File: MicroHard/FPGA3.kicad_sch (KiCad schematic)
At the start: 19 parts, among them J4 FPGA_DEBUG, U5 XC7A100T-FTG256

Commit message: feat: completed schematic draft
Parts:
- J4: footprint (none) -> MicroHard:MOLEX_87832-1420
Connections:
- net DONE renamed FPGA_DONE
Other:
- note removed: "Are these pull ups neccessary"
- note removed: "Very unsure here"
- moved on the sheet: D2, R22, TP2
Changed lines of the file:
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@@
 	)
 	(junction
-		(at 160.02 69.85)
+		(at 156.21 69.85)
 		(diameter 0)
 		(color 0 0 0 0)
@@
 	(wire
 		(pts
-			(xy 175.26 53.34) (xy 175.26 24.13)
+			(xy 151.13 69.85) (xy 156.21 69.85)
 		)
 		(stroke
@@
 	(wire
 		(pts
-			(xy 69.85 147.32) (xy 76.2 147.32)
+			(xy 175.26 53.34) (xy 175.26 24.13)
 		)
 		(stroke
@@
 	(wire
 		(pts
-			(xy 160.02 66.04) (xy 160.02 69.85)
+			(xy 69.85 147.32) (xy 76.2 147.32)
 		)
 		(stroke
@@
 	(wire
 		(pts
-			(xy 38.1 154.94) (xy 48.26 154.94)
+			(xy 156.21 66.04) (xy 156.21 69.85)
 		)
 		(stroke
@@
 	(wire
 		(pts
-			(xy 148.59 74.93) (xy 153.67 74.93)
+			(xy 38.1 154.94) (xy 48.26 154.94)
 		)
 		(stroke
@@
 	(wire
 		(pts
-			(xy 151.13 69.85) (xy 160.02 69.85)
+			(xy 148.59 74.93) (xy 153.67 74.93)
 		)
 		(stroke
@@
 	(wire
 		(pts
-			(xy 160.02 69.85) (xy 167.64 69.85)
+			(xy 156.21 69.85) (xy 158.75 69.85)
 		)
 		(stroke
@@
 	(wire
 		(pts
-			(xy 59.69 125.73) (xy 66.04 125.73)
+			(xy 66.04 129.54) (xy 72.39 129.54)
 		)
 		(stroke
@@
 	(wire
 		(pts
-			(xy 29.21 125.73) (xy 39.37 125.73)
+			(xy 38.1 129.54) (xy 45.72 129.54)
 		)
 		(stroke
@@
 	(wire
 		(pts
-			(xy 52.07 125.73) (xy 46.99 125.73)
+			(xy 58.42 129.54) (xy 53.34 129.54)
 		)
 		(stroke
@@
 	(wire
 		(pts
-			(xy 107.95 57.15) (xy 118.11 57.15)
+			(xy 107.95 57.15) (xy 116.84 57.15)
 		)
 		(stroke
@@
 		)
 	)
-	(text "Very unsure here\n"
-		(exclude_from_sim no)
-		(at 157.226 99.314 0)
-		(effects
-			(font
-				(size 1.27 1.27)
-			)
-		)
-	)
-	(text "Are these pull ups neccessary"
-		(exclude_from_sim no)
-		(at 235.712 49.276 0)
-		(effects
-			(font
-				(size 1.27 1.27)
-			)
-		)
-	)
 	(label "JTAG_TDI"
 		(at 115.57 44.45 0)
@@
 		)
 	)
+	(label "VCC0_0"
+		(at 252.73 49.53 90)
+		(fields_autoplaced yes)
+		(effects
+			(font
+				(size 1.27 1.27)
+			)
+			(justify left bottom)
+		)
+	)
 	(label "JTAG_TDI"
 		(at 227.33 73.66 180)
@@
 		)
 	)
-	(label "DONE"
-		(at 29.21 125.73 180)
+	(label "VCC0_0"
+		(at 118.11 80.01 0)
 		(fields_autoplaced yes)
 		(effects
@@
 				(size 1.27 1.27)
 			)
-			(justify right bottom)
+			(justify left bottom)
 		)
 	)
-	(label "DONE"
-		(at 167.64 69.85 0)
+	(label "VCC0_0"
+		(at 167.64 92.71 0)
 		(fields_autoplaced yes)
 		(effects
@@
 		)
 	)
-	(label "VCC0_0"
-		(at 167.64 92.71 0)
+	(global_label "FPGA_DONE"
+		(shape output)
+		(at 158.75 69.85 0)
 		(fields_autoplaced yes)
 		(effects
@@
 				(size 1.27 1.27)
 			)
-			(justify left bottom)
+			(justify left)
+		)
+		(property "Intersheetrefs" "${INTERSHEET_REFS}"
+			(at 172.5 69.85 0)
+			(effects
+				(font
+					(size 1.27 1.27)
+				)
+				(justify left)
+				(hide yes)
+			)
 		)
 	)
@@
 		)
 	)
-	(global_label "+3.3V"
+	(global_label "FPGA_LED2"
 		(shape input)
-		(at 118.11 80.01 0)
+		(at 38.1 154.94 180)
 		(fields_autoplaced yes)
 		(effects
@@
 				(size 1.27 1.27)
 			)
-			(justify left)
+			(justify right)
 		)
 		(property "Intersheetrefs" "${INTERSHEET_REFS}"
-			(at 126.78 80.01 0)
+			(at 24.7734 154.94 0)
 			(effects
 				(font
 					(size 1.27 1.27)
 				)
-				(justify left)
+				(justify right)
 				(hide yes)
 			)
 		)
 	)
-	(global_label "FPGA_LED2"
+	(global_label "FPGA_DONE"
 		(shape input)
-		(at 38.1 154.94 180)
+		(at 38.1 129.54 180)
 		(fields_autoplaced yes)
 		(effects
@@
 		)
 		(property "Intersheetrefs" "${INTERSHEET_REFS}"
-			(at 24.7734 154.94 0)
+			(at 24.35 129.54 0)
 			(effects
 				(font
@@
 		)
 	)
-	(global_label "+3.3V"
+	(global_label "FPGA_LED1"
 		(shape input)
-		(at 252.73 49.53 90)
+		(at 38.1 147.32 180)
 		(fields_autoplaced yes)
 		(effects
@@
 				(size 1.27 1.27)
 			)
-			(justify left)
+			(justify right)
 		)
 		(property "Intersheetrefs" "${INTERSHEET_REFS}"
-			(at 252.73 40.86 90)
+			(at 24.7734 147.32 0)
 			(effects
 				(font
 					(size 1.27 1.27)
 				)
-				(justify left)
+				(justify right)
 				(hide yes)
 			)
 		)
 	)
-	(global_label "FPGA_LED1"
-		(shape input)
-		(at 38.1 147.32 180)
+	(global_label "FPGA_CONFIG_CLOCK"
+		(shape output)
+		(at 116.84 57.15 0)
 		(fields_autoplaced yes)
 		(effects
@@
 				(size 1.27 1.27)
 			)
-			(justify right)
+			(justify left)
 		)
 		(property "Intersheetrefs" "${INTERSHEET_REFS}"
-			(at 24.7734 147.32 0)
+			(at 139.5406 57.15 0)
 			(effects
 				(font
 					(size 1.27 1.27)
 				)
-				(justify right)
+				(justify left)
 				(hide yes)
 			)
 		)
 	)
-	(hierarchical_label "FPGA_CONFIG_CLOCK"
-		(shape input)
-		(at 118.11 57.15 0)
-		(fields_autoplaced yes)
-		(effects
-			(font
-				(size 1.27 1.27)
-			)
-			(justify left)
-		)
-	)
 	(hierarchical_label "FPGA_RESET"
 		(shape input)
@@
 	(symbol
 		(lib_id "Device:R")
-		(at 43.18 125.73 90)
+		(at 49.53 129.54 90)
 		(unit 1)
 		(exclude_from_sim no)
@@
 		(fields_autoplaced yes)
 		(property "Reference" "R22"
-			(at 43.18 119.38 90)
+			(at 49.53 123.19 90)
 			(effects
 				(font
@@
 		)
 		(property "Value" "100"
-			(at 43.18 121.92 90)
+			(at 49.53 125.73 90)
 			(effects
 				(font
@@
 		)
 		(property "Footprint" ""
-			(at 43.18 127.508 90)
+			(at 49.53 131.318 90)
 			(effects
 				(font
@@
 		)
 		(property "Datasheet" "~"
-			(at 43.18 125.73 0)
+			(at 49.53 129.54 0)
 			(effects
 				(font
@@
 		)
 		(property "Description" "Resistor"
-			(at 43.18 125.73 0)
+			(at 49.53 129.54 0)
 			(effects
 				(font
@@
 	(symbol
 		(lib_id "Device:LED")
-		(at 55.88 125.73 180)
+		(at 62.23 129.54 180)
 		(unit 1)
 		(exclude_from_sim no)
@@
 		(fields_autoplaced yes)
 		(property "Reference" "D2"
-			(at 57.4675 118.11 0)
+			(at 63.8175 121.92 0)
 			(effects
 				(font
@@
 		)
 		(property "Value" "LED"
-			(at 57.4675 120.65 0)
+			(at 63.8175 124.46 0)
 			(effects
 				(font
@@
 		)
 		(property "Footprint" ""
-			(at 55.88 125.73 0)
+			(at 62.23 129.54 0)
 			(effects
 				(font
@@
 		)
 		(property "Datasheet" "~"
-			(at 55.88 125.73 0)
+			(at 62.23 129.54 0)
 			(effects
 				(font
@@
 		)
 		(property "Description" "Light emitting diode"
-			(at 55.88 125.73 0)
+			(at 62.23 129.54 0)
 			(effects
 				(font
@@
 	(symbol
 		(lib_id "power:GND")
-		(at 66.04 125.73 90)
+		(at 72.39 129.54 90)
 		(unit 1)
 		(exclude_from_sim no)
@@
 		(fields_autoplaced yes)
 		(property "Reference" "#PWR031"
-			(at 72.39 125.73 0)
+			(at 78.74 129.54 0)
 			(effects
 				(font
@@
 		)
 		(property "Value" "GND"
-			(at 69.85 125.7299 90)
+			(at 76.2 129.5399 90)
 			(effects
 				(font
@@
 		)
 		(property "Footprint" ""
-			(at 66.04 125.73 0)
+			(at 72.39 129.54 0)
 			(effects
 				(font
@@
 		)
 		(property "Datasheet" ""
-			(at 66.04 125.73 0)
+			(at 72.39 129.54 0)
 			(effects
 				(font
@@
 		)
 		(property "Description" "Power symbol creates a global label with name \"GND\" , ground"
-			(at 66.04 125.73 0)
+			(at 72.39 129.54 0)
 			(effects
 				(font
@@
 			)
 		)
-		(property "Footprint" ""
+		(property "Footprint" "MicroHard:MOLEX_87832-1420"
 			(at 270.51 71.12 0)
 			(effects
@@
 	(symbol
 		(lib_id "Connector:TestPoint")
-		(at 160.02 66.04 0)
+		(at 156.21 66.04 0)
 		(unit 1)
 		(exclude_from_sim no)
@@
 		(fields_autoplaced yes)
 		(property "Reference" "TP2"
-			(at 162.56 61.4679 0)
+			(at 158.75 61.4679 0)
 			(effects
 				(font
@@
 		)
 		(property "Value" "TestPoint"
-			(at 162.56 64.0079 0)
+			(at 158.75 64.0079 0)
 			(effects
 				(font
@@
 		)
 		(property "Footprint" ""
-			(at 165.1 66.04 0)
+			(at 161.29 66.04 0)
 			(effects
 				(font
@@
 		)
 		(property "Datasheet" "~"
-			(at 165.1 66.04 0)
+			(at 161.29 66.04 0)
 			(effects
 				(font
@@
 		)
 		(property "Description" "test point"
-			(at 160.02 66.04 0)
+			(at 156.21 66.04 0)
 			(effects
 				(font

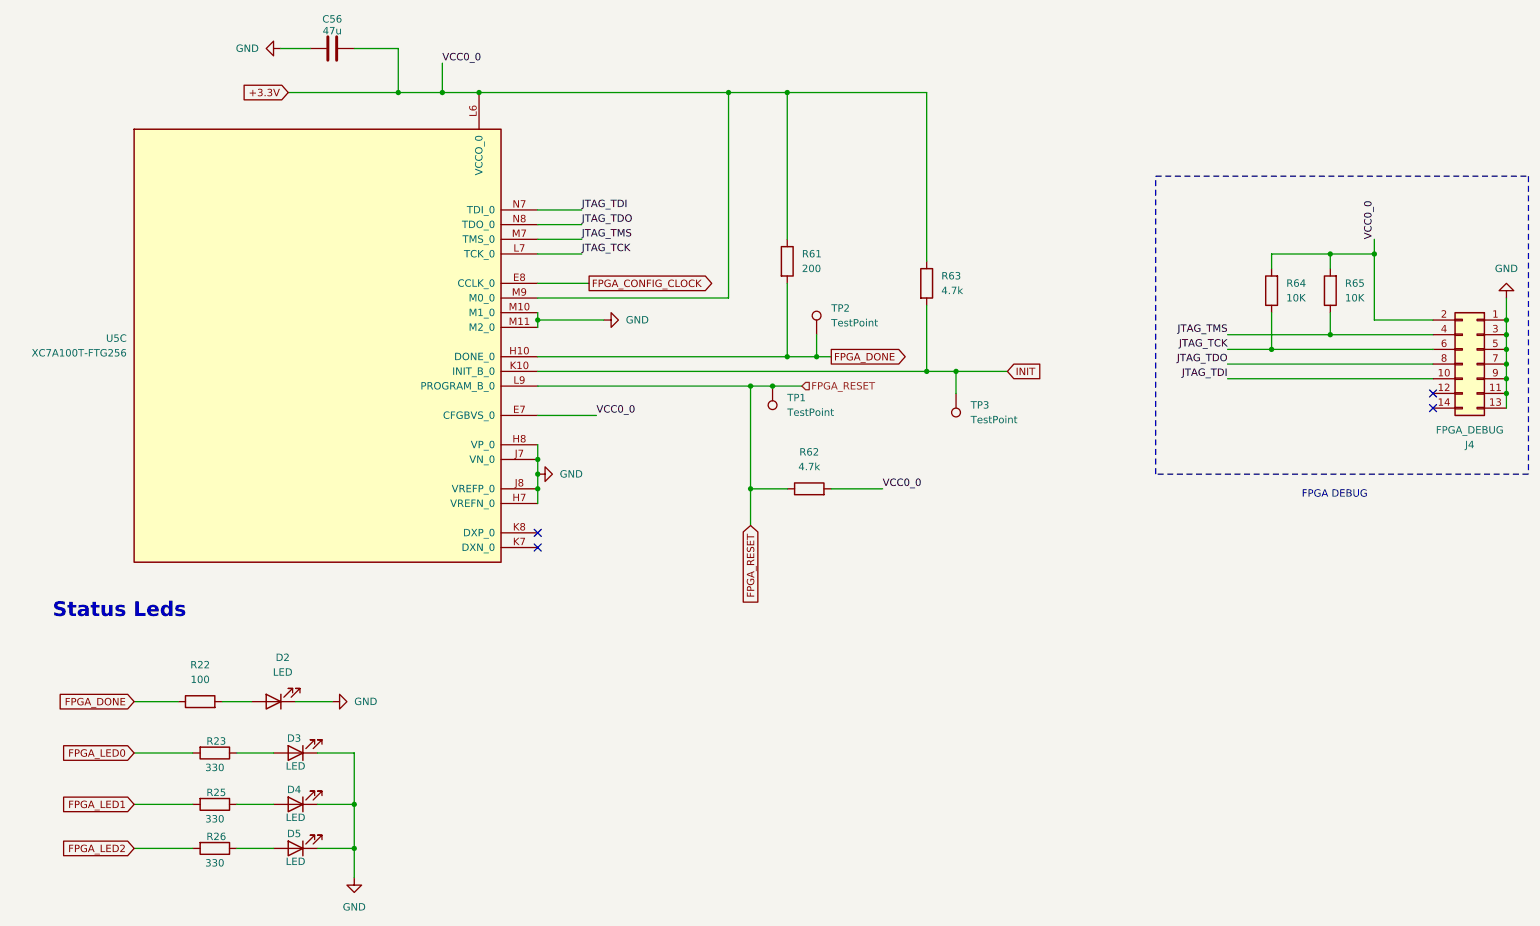
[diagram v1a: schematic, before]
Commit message: Renumber parts
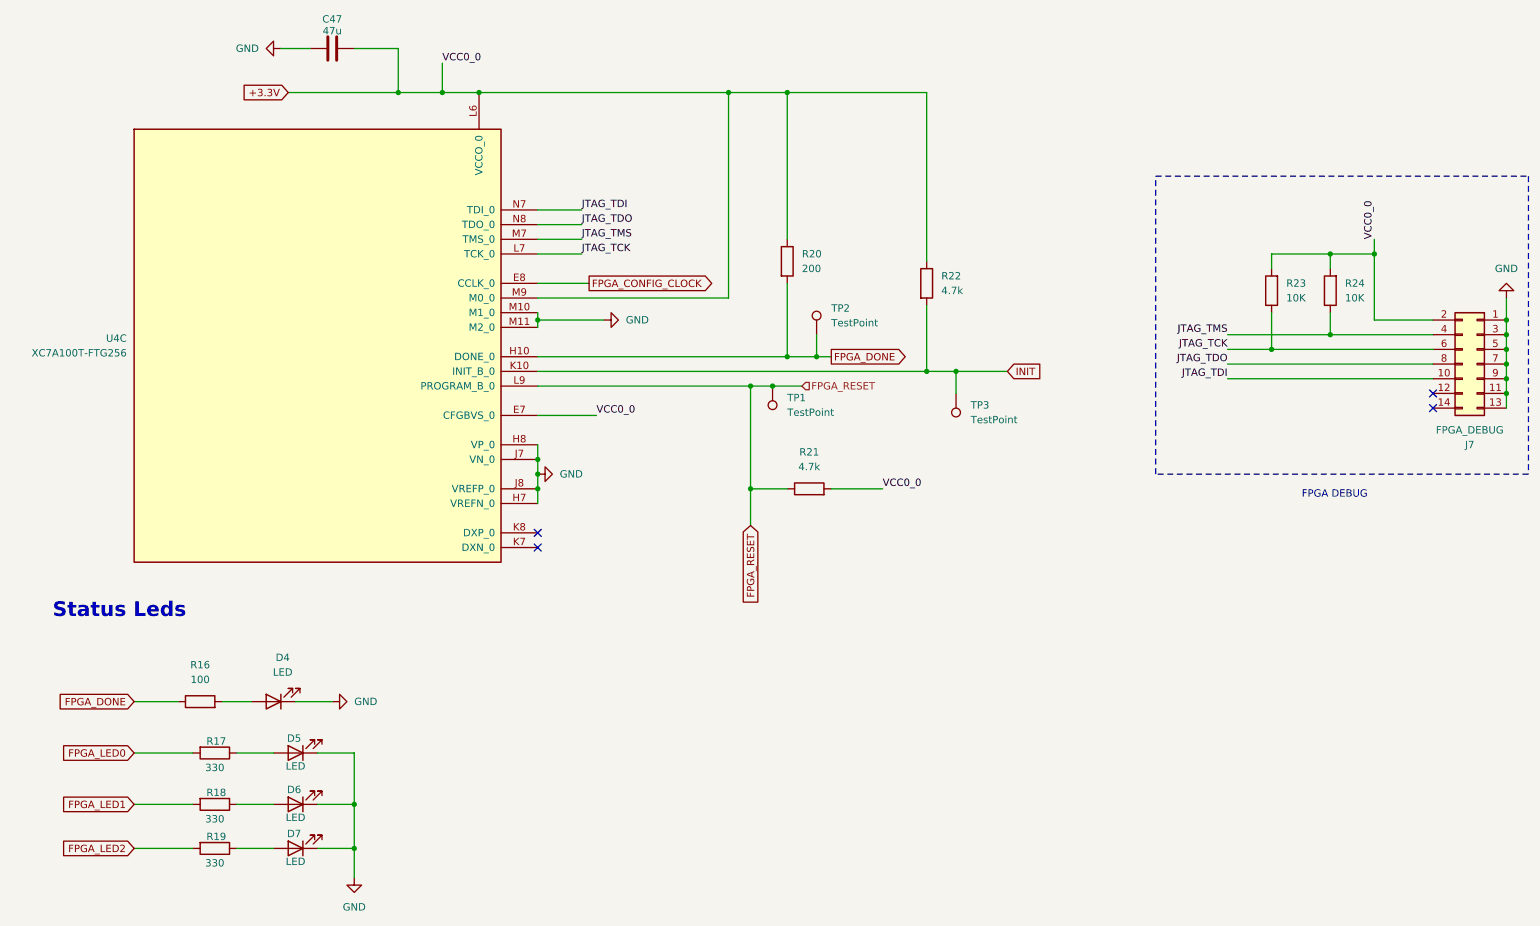
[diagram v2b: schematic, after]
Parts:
- renumbered C56 to C47, D2 to D4, D3 to D5, D4 to D6, D5 to D7, J4 to J7, R22 to R16, R23 to R17, R25 to R18, R26 to R19, R61 to R20, R62 to R21, R63 to R22, R64 to R23, R65 to R24, U5 to U4
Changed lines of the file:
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@@
 		(dnp no)
 		(fields_autoplaced yes)
-		(property "Reference" "R63"
+		(property "Reference" "R22"
 			(at 177.8 55.8799 0)
 			(effects
@@
 			(project ""
 				(path "/578bd531-a491-4b15-a479-460d159ffc14/e381883e-e672-4900-88a5-08b94f970a88/5897012d-c01f-459a-b65a-eba111a7dafb"
-					(reference "R63")
+					(reference "R22")
 					(unit 1)
 				)
@@
 		(dnp no)
 		(fields_autoplaced yes)
-		(property "Reference" "R61"
+		(property "Reference" "R20"
 			(at 153.67 52.0699 0)
 			(effects
@@
 			(project ""
 				(path "/578bd531-a491-4b15-a479-460d159ffc14/e381883e-e672-4900-88a5-08b94f970a88/5897012d-c01f-459a-b65a-eba111a7dafb"
-					(reference "R61")
+					(reference "R20")
 					(unit 1)
 				)
@@
 		(dnp no)
 		(fields_autoplaced yes)
-		(property "Reference" "R64"
+		(property "Reference" "R23"
 			(at 237.49 57.1499 0)
 			(effects
@@
 			(project ""
 				(path "/578bd531-a491-4b15-a479-460d159ffc14/e381883e-e672-4900-88a5-08b94f970a88/5897012d-c01f-459a-b65a-eba111a7dafb"
-					(reference "R64")
+					(reference "R23")
 					(unit 1)
 				)
@@
 		(dnp no)
 		(fields_autoplaced yes)
-		(property "Reference" "R22"
+		(property "Reference" "R16"
 			(at 49.53 123.19 90)
 			(effects
@@
 			(project ""
 				(path "/578bd531-a491-4b15-a479-460d159ffc14/e381883e-e672-4900-88a5-08b94f970a88/5897012d-c01f-459a-b65a-eba111a7dafb"
-					(reference "R22")
+					(reference "R16")
 					(unit 1)
 				)
@@
 		(on_board yes)
 		(dnp no)
-		(property "Reference" "R26"
+		(property "Reference" "R19"
 			(at 52.324 152.908 90)
 			(effects
@@
 			(project "MicroHard"
 				(path "/578bd531-a491-4b15-a479-460d159ffc14/e381883e-e672-4900-88a5-08b94f970a88/5897012d-c01f-459a-b65a-eba111a7dafb"
-					(reference "R26")
+					(reference "R19")
 					(unit 1)
 				)
@@
 		(dnp no)
 		(fields_autoplaced yes)
-		(property "Reference" "#PWR032"
+		(property "Reference" "#PWR035"
 			(at 76.2 166.37 0)
 			(effects
@@
 			(project ""
 				(path "/578bd531-a491-4b15-a479-460d159ffc14/e381883e-e672-4900-88a5-08b94f970a88/5897012d-c01f-459a-b65a-eba111a7dafb"
-					(reference "#PWR032")
+					(reference "#PWR035")
 					(unit 1)
 				)
@@
 		(dnp no)
 		(fields_autoplaced yes)
-		(property "Reference" "D2"
+		(property "Reference" "D4"
 			(at 63.8175 121.92 0)
 			(effects
@@
 			(project ""
 				(path "/578bd531-a491-4b15-a479-460d159ffc14/e381883e-e672-4900-88a5-08b94f970a88/5897012d-c01f-459a-b65a-eba111a7dafb"
-					(reference "D2")
+					(reference "D4")
 					(unit 1)
 				)
@@
 		(on_board yes)
 		(dnp no)
-		(property "Reference" "C56"
+		(property "Reference" "C47"
 			(at 72.39 11.43 90)
 			(effects
@@
 			(project "MicroHard"
 				(path "/578bd531-a491-4b15-a479-460d159ffc14/e381883e-e672-4900-88a5-08b94f970a88/5897012d-c01f-459a-b65a-eba111a7dafb"
-					(reference "C56")
+					(reference "C47")
 					(unit 1)
 				)
@@
 		(dnp no)
 		(fields_autoplaced yes)
-		(property "Reference" "#PWR031"
+		(property "Reference" "#PWR034"
 			(at 78.74 129.54 0)
 			(effects
@@
 			(project ""
 				(path "/578bd531-a491-4b15-a479-460d159ffc14/e381883e-e672-4900-88a5-08b94f970a88/5897012d-c01f-459a-b65a-eba111a7dafb"
-					(reference "#PWR031")
+					(reference "#PWR034")
 					(unit 1)
 				)
@@
 		(on_board yes)
 		(dnp no)
-		(property "Reference" "J4"
+		(property "Reference" "J7"
 			(at 269.24 85.09 0)
 			(effects
@@
 			(project ""
 				(path "/578bd531-a491-4b15-a479-460d159ffc14/e381883e-e672-4900-88a5-08b94f970a88/5897012d-c01f-459a-b65a-eba111a7dafb"
-					(reference "J4")
+					(reference "J7")
 					(unit 1)
 				)
@@
 		(dnp no)
 		(fields_autoplaced yes)
-		(property "Reference" "R62"
+		(property "Reference" "R21"
 			(at 154.94 86.36 90)
 			(effects
@@
 			(project "MicroHard"
 				(path "/578bd531-a491-4b15-a479-460d159ffc14/e381883e-e672-4900-88a5-08b94f970a88/5897012d-c01f-459a-b65a-eba111a7dafb"
-					(reference "R62")
+					(reference "R21")
 					(unit 1)
 				)
@@
 		(on_board yes)
 		(dnp no)
-		(property "Reference" "D5"
+		(property "Reference" "D7"
 			(at 65.786 152.4 0)
 			(effects
@@
 			(project "MicroHard"
 				(path "/578bd531-a491-4b15-a479-460d159ffc14/e381883e-e672-4900-88a5-08b94f970a88/5897012d-c01f-459a-b65a-eba111a7dafb"
-					(reference "D5")
+					(reference "D7")
 					(unit 1)
 				)
@@
 		(dnp no)
 		(fields_autoplaced yes)
-		(property "Reference" "U5"
+		(property "Reference" "U4"
 			(at 36.83 66.6749 0)
 			(effects
@@
 			(project "MicroHard"
 				(path "/578bd531-a491-4b15-a479-460d159ffc14/e381883e-e672-4900-88a5-08b94f970a88/5897012d-c01f-459a-b65a-eba111a7dafb"
-					(reference "U5")
+					(reference "U4")
 					(unit 3)
 				)
@@
 		(on_board yes)
 		(dnp no)
-		(property "Reference" "R25"
+		(property "Reference" "R18"
 			(at 52.324 145.288 90)
 			(effects
@@
 			(project "MicroHard"
 				(path "/578bd531-a491-4b15-a479-460d159ffc14/e381883e-e672-4900-88a5-08b94f970a88/5897012d-c01f-459a-b65a-eba111a7dafb"
-					(reference "R25")
+					(reference "R18")
 					(unit 1)
 				)
@@
 		(dnp no)
 		(fields_autoplaced yes)
-		(property "Reference" "#PWR033"
+		(property "Reference" "#PWR036"
 			(at 114.3 90.17 0)
 			(effects
@@
 			(project ""
 				(path "/578bd531-a491-4b15-a479-460d159ffc14/e381883e-e672-4900-88a5-08b94f970a88/5897012d-c01f-459a-b65a-eba111a7dafb"
-					(reference "#PWR033")
+					(reference "#PWR036")
 					(unit 1)
 				)
@@
 		(dnp no)
 		(fields_autoplaced yes)
-		(property "Reference" "#PWR035"
+		(property "Reference" "#PWR037"
 			(at 125.73 63.5 0)
 			(effects
@@
 			(project ""
 				(path "/578bd531-a491-4b15-a479-460d159ffc14/e381883e-e672-4900-88a5-08b94f970a88/5897012d-c01f-459a-b65a-eba111a7dafb"
-					(reference "#PWR035")
+					(reference "#PWR037")
 					(unit 1)
 				)
@@
 		(on_board yes)
 		(dnp no)
-		(property "Reference" "D3"
+		(property "Reference" "D5"
 			(at 65.786 135.89 0)
 			(effects
@@
 			(project "MicroHard"
 				(path "/578bd531-a491-4b15-a479-460d159ffc14/e381883e-e672-4900-88a5-08b94f970a88/5897012d-c01f-459a-b65a-eba111a7dafb"
-					(reference "D3")
+					(reference "D5")
 					(unit 1)
 				)
@@
 		(dnp no)
 		(fields_autoplaced yes)
-		(property "Reference" "#PWR030"
+		(property "Reference" "#PWR033"
 			(at 57.15 16.51 0)
 			(effects
@@
 			(project ""
 				(path "/578bd531-a491-4b15-a479-460d159ffc14/e381883e-e672-4900-88a5-08b94f970a88/5897012d-c01f-459a-b65a-eba111a7dafb"
-					(reference "#PWR030")
+					(reference "#PWR033")
 					(unit 1)
 				)
@@
 		(dnp no)
 		(fields_autoplaced yes)
-		(property "Reference" "R65"
+		(property "Reference" "R24"
 			(at 247.65 57.1499 0)
 			(effects
@@
 			(project "MicroHard"
 				(path "/578bd531-a491-4b15-a479-460d159ffc14/e381883e-e672-4900-88a5-08b94f970a88/5897012d-c01f-459a-b65a-eba111a7dafb"
-					(reference "R65")
+					(reference "R24")
 					(unit 1)
 				)
@@
 		(on_board yes)
 		(dnp no)
-		(property "Reference" "D4"
+		(property "Reference" "D6"
 			(at 65.786 144.78 0)
 			(effects
@@
 			(project "MicroHard"
 				(path "/578bd531-a491-4b15-a479-460d159ffc14/e381883e-e672-4900-88a5-08b94f970a88/5897012d-c01f-459a-b65a-eba111a7dafb"
-					(reference "D4")
+					(reference "D6")
 					(unit 1)
 				)
@@
 		(on_board yes)
 		(dnp no)
-		(property "Reference" "R23"
+		(property "Reference" "R17"
 			(at 52.324 136.398 90)
 			(effects
@@
 			(project ""
 				(path "/578bd531-a491-4b15-a479-460d159ffc14/e381883e-e672-4900-88a5-08b94f970a88/5897012d-c01f-459a-b65a-eba111a7dafb"
-					(reference "R23")
-					(unit 1)
-				)
+					(reference "R17")
+					(unit 1)
+				)

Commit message: footprints
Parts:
- C47: footprint (none) -> Capacitor_SMD:C_1210_3225Metric_Pad1.33x2.70mm_HandSolder
- D4, D5, D6, D7: footprint (none) -> LED_SMD:LED_1206_3216Metric_Pad1.42x1.75mm_HandSolder
- R16, R17, R18, R19, R20, R21, R22: footprint (none) -> Resistor_SMD:R_1206_3216Metric_Pad1.30x1.75mm_HandSolder
- R23, R24: value 10K -> 10k; footprint (none) -> Resistor_SMD:R_1206_3216Metric_Pad1.30x1.75mm_HandSolder

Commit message: Small fixes
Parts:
- TP1, TP2, TP3: footprint (none) -> TestPoint:TestPoint_Pad_D2.0mm
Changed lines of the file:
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@@
 			)
 		)
-		(property "Footprint" ""
+		(property "Footprint" "TestPoint:TestPoint_Pad_D2.0mm"
 			(at 175.26 76.2 0)
 			(effects
@@
 			)
 		)
-		(property "Footprint" ""
+		(property "Footprint" "TestPoint:TestPoint_Pad_D2.0mm"
 			(at 143.51 74.93 0)
 			(effects
@@
 			)
 		)
-		(property "Footprint" ""
+		(property "Footprint" "TestPoint:TestPoint_Pad_D2.0mm"
 			(at 161.29 66.04 0)
 			(effects
